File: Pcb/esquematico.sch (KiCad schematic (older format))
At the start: 23 parts, among them J1 Jack-DC, J2 Pin_Header, J3 Conn_01x02, J4 USB_B, J5 Conn_01x03, J6 Pin_Header, SW1 SW_Push, U1 L7805, U2 AZ1117-3.3, U3 PIC18F4550-IP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

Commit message: correcciones de errores de conexion
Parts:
- added C7: 220nF, Capacitor_THT:CP_Radial_Tantal_D5.0mm_P5.00mm, symbol Device:CP1
- D1: footprint Diode_THT:D_A-405_P7.62mm_Horizontal -> Diode_THT:D_DO-41_SOD81_P7.62mm_Horizontal
- D2, D3: footprint LED_THT:LED_D3.0mm_Clear -> LED_THT:LED_D3.0mm
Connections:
- net GND: now also J2.1 (Pin_1), C7.2; no longer U3.18 (VUSB)
- net RESET: no longer J2.1 (Pin_1)
- new net: C7.1, U3.18 (VUSB)
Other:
- moved on the sheet: J5
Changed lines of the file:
@@
 F 0 "D1" H 1500 6183 50  0000 C CNN
 F 1 "1N4004" H 1500 6274 50  0000 C CNN
-F 2 "Diode_THT:D_A-405_P7.62mm_Horizontal" H 1500 6400 50  0001 C CNN
+F 2 "Diode_THT:D_DO-41_SOD81_P7.62mm_Horizontal" H 1500 6400 50  0001 C CNN
 F 3 "~" H 1500 6400 50  0001 C CNN
 	1    1500 6400
@@
 Connection ~ 2000 6400
 Wire Wire Line
-	2000 6400 2350 6400
-Wire Wire Line
 	3300 6600 3300 6400
-Wire Wire Line
-	3300 6400 2950 6400
 $Comp
 L power:GND #PWR03
@@
 $EndComp
 Wire Wire Line
-	1050 6600 1050 7150
-Wire Wire Line
 	2000 6900 2000 7150
 Wire Wire Line
@@
 L Connector_Generic:Conn_01x03 J5
 U 1 1 5F8EF2AF
-P 7600 6300
-F 0 "J5" H 7680 6342 50  0000 L CNN
-F 1 "Conn_01x03" H 7680 6251 50  0000 L CNN
-F 2 "Connector_PinSocket_2.54mm:PinSocket_1x03_P2.54mm_Vertical" H 7600 6300 50  0001 C CNN
-F 3 "~" H 7600 6300 50  0001 C CNN
-	1    7600 6300
-	1    0    0    -1
-$EndComp
-Text Label 7250 5700 2    50   ~ 0
+P 8000 6300
+F 0 "J5" H 8080 6342 50  0000 L CNN
+F 1 "Conn_01x03" H 8080 6251 50  0000 L CNN
+F 2 "Connector_PinSocket_2.54mm:PinSocket_1x03_P2.54mm_Vertical" H 8000 6300 50  0001 C CNN
+F 3 "~" H 8000 6300 50  0001 C CNN
+	1    8000 6300
+	1    0    0    -1
+$EndComp
+Text Label 7650 5700 2    50   ~ 0
 +5V_EXT
-Text Label 6750 5700 2    50   ~ 0
+Text Label 7150 5700 2    50   ~ 0
 +5V
-Text Label 6250 5700 2    50   ~ 0
+Text Label 6450 5700 2    50   ~ 0
 +5V_USB
 Wire Wire Line
-	7400 6200 7250 6200
-Wire Wire Line
-	7250 6200 7250 5700
-Wire Wire Line
-	7400 6300 6750 6300
-Wire Wire Line
-	6750 6300 6750 5700
-Wire Wire Line
-	6250 5700 6250 6400
-Wire Wire Line
-	6250 6400 7400 6400
+	7800 6200 7650 6200
+Wire Wire Line
+	7650 6200 7650 5700
+Wire Wire Line
+	7800 6300 7150 6300
+Wire Wire Line
+	7150 6300 7150 5700
+Wire Wire Line
+	6450 5700 6450 6400
+Wire Wire Line
+	6450 6400 7800 6400
 $Comp
 L MCU_Microchip_PIC18:PIC18F4550-IP U3
@@
 Wire Wire Line
 	4400 2800 4600 2800
-$Comp
-L power:GND #PWR06
-U 1 1 5F9AE0CD
-P 2900 4500
-F 0 "#PWR06" H 2900 4250 50  0001 C CNN
-F 1 "GND" H 2905 4327 50  0000 C CNN
-F 2 "" H 2900 4500 50  0001 C CNN
-F 3 "" H 2900 4500 50  0001 C CNN
-	1    2900 4500
-	1    0    0    -1
-$EndComp
-Wire Wire Line
-	4600 3000 2900 3000
-Wire Wire Line
-	2900 3000 2900 4500
 Text Label 4400 3800 2    50   ~ 0
 PIN10
@@
 Text Label 3350 3400 2    50   ~ 0
 +5V_USB
-Wire Wire Line
-	3350 3400 3350 3900
 $Comp
 L power:GND #PWR09
@@
 	1    0    0    -1
 $EndComp
-Wire Wire Line
-	4400 4550 4400 4300
-Wire Wire Line
-	4400 4200 3950 4200
-Wire Wire Line
-	3950 4300 4400 4300
-Connection ~ 4400 4300
-Wire Wire Line
-	4400 4300 4400 4200
 $Comp
 L Device:Crystal Y1
@@
 $EndComp
 Wire Wire Line
-	8500 4350 8250 4350
-Wire Wire Line
-	8000 4350 7950 4300
+	8550 4350 8250 4350
+Wire Wire Line
+	7950 4350 7950 4300
 Wire Wire Line
 	7950 4000 7950 3850
@@
 Connection ~ 8250 4350
 Wire Wire Line
-	8250 4350 8000 4350
+	8250 4350 7950 4350
 Wire Wire Line
 	6800 3000 8550 3000
@@
 F 0 "D3" V 9639 4782 50  0000 R CNN
 F 1 "LED_RUN" V 9548 4782 50  0000 R CNN
-F 2 "LED_THT:LED_D3.0mm_Clear" H 9600 4900 50  0001 C CNN
+F 2 "LED_THT:LED_D3.0mm" H 9600 4900 50  0001 C CNN
 F 3 "~" H 9600 4900 50  0001 C CNN
 	1    9600 4900
@@
 $EndComp
 Wire Wire Line
-	8550 4300 8500 4350
+	8550 4300 8550 4350
 Wire Wire Line
 	8550 3850 8550 4000
@@
 F 0 "D2" V 9189 4979 50  0000 L CNN
 F 1 "LED_POWER" V 9098 4979 50  0000 L CNN
-F 2 "LED_THT:LED_D3.0mm_Clear" H 9150 4900 50  0001 C CNN
+F 2 "LED_THT:LED_D3.0mm" H 9150 4900 50  0001 C CNN
 F 3 "~" H 9150 4900 50  0001 C CNN
 	1    9150 4900
@@
 Text Notes 850  5900 0    70   ~ 0
 Conexion Jack con voltage regulado a 5V
-Text Notes 3700 5900 0    70   ~ 0
+Text Notes 4100 5900 0    70   ~ 0
 Voltage regulado con salida a 3.3V
-Wire Wire Line
-	1450 950  1650 950
-Text Label 1650 950  0    50   ~ 0
-RESET
 Connection ~ 2550 2050
 Wire Wire Line
@@
 Text Notes 10250 6200 2    70   ~ 0
 Indicadores led de arranque y poder
+Wire Wire Line
+	2950 6400 3300 6400
+Wire Wire Line
+	2900 3000 4600 3000
+$Comp
+L power:GND #PWR0101
+U 1 1 5F8FF478
+P 2900 4500
+F 0 "#PWR0101" H 2900 4250 50  0001 C CNN
+F 1 "GND" H 2905 4327 50  0000 C CNN
+F 2 "" H 2900 4500 50  0001 C CNN
+F 3 "" H 2900 4500 50  0001 C CNN
+	1    2900 4500
+	1    0    0    -1
+$EndComp
+Wire Wire Line
+	2550 950  2550 1450
+Wire Wire Line
+	1450 950  2550 950
+Connection ~ 2550 1450
+Wire Wire Line
+	1050 6600 1050 7150
+Wire Wire Line
+	4400 4200 4400 4300
+Wire Wire Line
+	3950 4200 4400 4200
+Wire Wire Line
+	3950 4300 4400 4300
+Connection ~ 4400 4300
+Wire Wire Line
+	4400 4300 4400 4550
+Wire Wire Line
+	3350 3400 3350 3900
+$Comp
+L power:PWR_FLAG #FLG0101
+U 1 1 5F9A1DEC
+P 2300 6100
+F 0 "#FLG0101" H 2300 6175 50  0001 C CNN
+F 1 "PWR_FLAG" H 2300 6273 50  0000 C CNN
+F 2 "" H 2300 6100 50  0001 C CNN
+F 3 "~" H 2300 6100 50  0001 C CNN
+	1    2300 6100
+	1    0    0    -1
+$EndComp
+Wire Wire Line
+	2300 6100 2300 6400
+Wire Wire Line
+	2000 6400 2300 6400
+Connection ~ 2300 6400
+Wire Wire Line
+	2300 6400 2350 6400
+$Comp
+L Device:CP1 C7
+U 1 1 5F9C7313
+P 2900 3800
+F 0 "C7" H 3015 3846 50  0000 L CNN
+F 1 "220nF" H 3015 3755 50  0000 L CNN
+F 2 "Capacitor_THT:CP_Radial_Tantal_D5.0mm_P5.00mm" H 2900 3800 50  0001 C CNN
+F 3 "~" H 2900 3800 50  0001 C CNN
+	1    2900 3800
+	1    0    0    -1
+$EndComp
+Wire Wire Line
+	2900 3000 2900 3650
+Wire Wire Line
+	2900 4500 2900 3950
+$Comp
+L power:PWR_FLAG #FLG0103
+U 1 1 5F8B7931
+P 6800 5700
+F 0 "#FLG0103" H 6800 5775 50  0001 C CNN
+F 1 "PWR_FLAG" H 6800 5873 50  0000 C CNN
+F 2 "" H 6800 5700 50  0001 C CNN
+F 3 "~" H 6800 5700 50  0001 C CNN
+	1    6800 5700
+	1    0    0    -1
+$EndComp
+Connection ~ 7150 6300
+Wire Wire Line
+	6800 6300 7150 6300
+Wire Wire Line
+	6800 5700 6800 6300
 $EndSCHEMATC

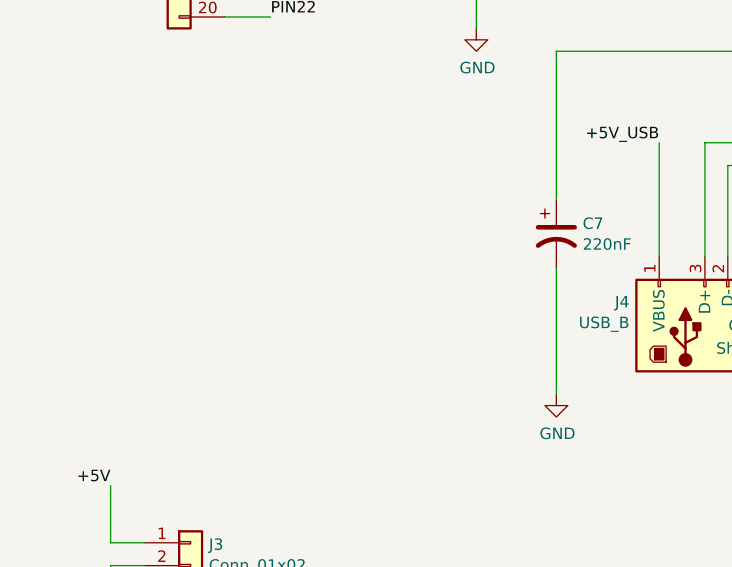
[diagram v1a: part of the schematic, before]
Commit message: se agrego datos faltantes al rotulo
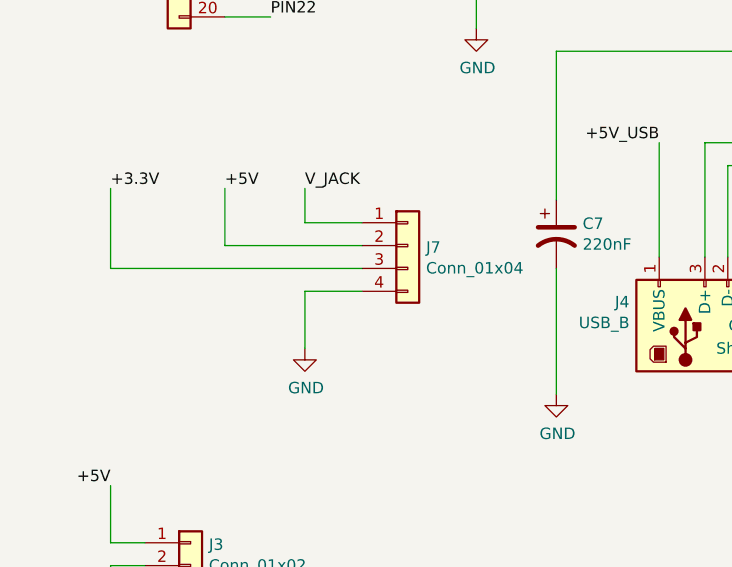
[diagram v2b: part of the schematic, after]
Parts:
- added J7: Conn_01x04, Connector_PinSocket_2.54mm:PinSocket_1x04_P2.54mm_Vertical, symbol Connector_Generic:Conn_01x04
- J5: footprint Connector_PinSocket_2.54mm:PinSocket_1x03_P2.54mm_Vertical -> Connector_PinHeader_2.54mm:PinHeader_1x03_P2.54mm_Vertical
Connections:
- net +3.3V: now also J7.3 (Pin_3)
- net +5V: now also J7.2 (Pin_2)
- net GND: now also J7.4 (Pin_4)
- net V_JACK: now also J7.1 (Pin_1)
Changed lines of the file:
@@
 encoding utf-8
 Sheet 1 1
-Title "Pinguino-PIC-CESE-DCI"
+Title "REPLICA-PLACA-PINGUINO-PIC"
 Date "2020-10-09"
-Rev ""
-Comp "Jose Mauricio Lara Tapia"
-Comment1 ""
-Comment2 ""
-Comment3 ""
+Rev "1.0"
+Comp ""
+Comment1 "Author: Ing. Jose Mauricio Lara Tapia"
+Comment2 "Reviewer: Raul Alejandro Camacho Dorado"
+Comment3 "Licencia BSD (proyecto CIAA), GPL o OHL (Cern"
 Comment4 ""
 $EndDescr
@@
 F 0 "J5" H 8080 6342 50  0000 L CNN
 F 1 "Conn_01x03" H 8080 6251 50  0000 L CNN
-F 2 "Connector_PinSocket_2.54mm:PinSocket_1x03_P2.54mm_Vertical" H 8000 6300 50  0001 C CNN
+F 2 "Connector_PinHeader_2.54mm:PinHeader_1x03_P2.54mm_Vertical" H 8000 6300 50  0001 C CNN
 F 3 "~" H 8000 6300 50  0001 C CNN
 	1    8000 6300
@@
 Wire Wire Line
 	6800 5700 6800 6300
+$Comp
+L Connector_Generic:Conn_01x04 J7
+U 1 1 5FA12738
+P 2250 3850
+F 0 "J7" H 2330 3842 50  0000 L CNN
+F 1 "Conn_01x04" H 2330 3751 50  0000 L CNN
+F 2 "Connector_PinSocket_2.54mm:PinSocket_1x04_P2.54mm_Vertical" H 2250 3850 50  0001 C CNN
+F 3 "~" H 2250 3850 50  0001 C CNN
+	1    2250 3850
+	1    0    0    -1
+$EndComp
+Text Label 1800 3600 0    50   ~ 0
+V_JACK
+$Comp
+L power:GND #PWR0102
+U 1 1 5FA3CE9A
+P 1800 4300
+F 0 "#PWR0102" H 1800 4050 50  0001 C CNN
+F 1 "GND" H 1805 4127 50  0000 C CNN
+F 2 "" H 1800 4300 50  0001 C CNN
+F 3 "" H 1800 4300 50  0001 C CNN
+	1    1800 4300
+	1    0    0    -1
+$EndComp
+Text Label 950  3600 0    50   ~ 0
++3.3V
+Wire Wire Line
+	1800 3600 1800 3750
+Wire Wire Line
+	1800 3750 2050 3750
+Wire Wire Line
+	950  3600 950  3950
+Wire Wire Line
+	950  3950 2050 3950
+Wire Wire Line
+	1800 4300 1800 4050
+Wire Wire Line
+	1800 4050 2050 4050
+Text Label 1450 3600 0    50   ~ 0
++5V
+Wire Wire Line
+	1450 3600 1450 3850
+Wire Wire Line
+	1450 3850 2050 3850
 $EndSCHEMATC

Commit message: ultimas correcciones
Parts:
- added H1, H2, H3, H4: MountingHole, MountingHole:MountingHole_2.2mm_M2_Pad_Via, symbol Mechanical:MountingHole
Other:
- note added: "AGUJEROS DE SUJECION"
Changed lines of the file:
@@
 $EndComp
-Wire Wire Line
-	4600 3400 3550 3400
 Wire Wire Line
 	3550 3400 3550 3900
 Wire Wire Line
 	3650 3900 3650 3500
-Wire Wire Line
-	3650 3500 4600 3500
 Text Label 3350 3400 2    50   ~ 0
 +5V_USB
@@
 Wire Wire Line
 	1450 3850 2050 3850
+Wire Wire Line
+	4600 3400 3550 3400
+Wire Wire Line
+	3650 3500 4600 3500
+$Comp
+L Mechanical:MountingHole H1
+U 1 1 5FAA90BD
+P 7750 1650
+F 0 "H1" H 7850 1696 50  0000 L CNN
+F 1 "MountingHole" H 7850 1605 50  0000 L CNN
+F 2 "MountingHole:MountingHole_2.2mm_M2_Pad_Via" H 7750 1650 50  0001 C CNN
+F 3 "~" H 7750 1650 50  0001 C CNN
+	1    7750 1650
+	1    0    0    -1
+$EndComp
+$Comp
+L Mechanical:MountingHole H3
+U 1 1 5FAAAF9C
+P 8600 1650
+F 0 "H3" H 8700 1696 50  0000 L CNN
+F 1 "MountingHole" H 8700 1605 50  0000 L CNN
+F 2 "MountingHole:MountingHole_2.2mm_M2_Pad_Via" H 8600 1650 50  0001 C CNN
+F 3 "~" H 8600 1650 50  0001 C CNN
+	1    8600 1650
+	1    0    0    -1
+$EndComp
+$Comp
+L Mechanical:MountingHole H2
+U 1 1 5FAB45A7
+P 7750 1950
+F 0 "H2" H 7850 1996 50  0000 L CNN
+F 1 "MountingHole" H 7850 1905 50  0000 L CNN
+F 2 "MountingHole:MountingHole_2.2mm_M2_Pad_Via" H 7750 1950 50  0001 C CNN
+F 3 "~" H 7750 1950 50  0001 C CNN
+	1    7750 1950
+	1    0    0    -1
+$EndComp
+$Comp
+L Mechanical:MountingHole H4
+U 1 1 5FABDE4C
+P 8600 1950
+F 0 "H4" H 8700 1996 50  0000 L CNN
+F 1 "MountingHole" H 8700 1905 50  0000 L CNN
+F 2 "MountingHole:MountingHole_2.2mm_M2_Pad_Via" H 8600 1950 50  0001 C CNN
+F 3 "~" H 8600 1950 50  0001 C CNN
+	1    8600 1950
+	1    0    0    -1
+$EndComp
+Text Notes 8100 1400 0    50   ~ 0
+AGUJEROS DE SUJECION
 $EndSCHEMATC
